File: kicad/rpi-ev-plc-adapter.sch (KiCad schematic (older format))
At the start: 51 parts, among them J1 Raspberry_RPI, J10 socket, J2 Conn_01x06, J3 header, J4 header, J5 header, J9 socket, M1 I2PLCAMN-ISE-002-T, M2 supply-5VtoPM12V_ebay-2530527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, SW1 push-button_ebay-183284526496, SW2 push-button_ebay-183284526496, SW5 dip-switch-6x2pos-smd-1.27mm

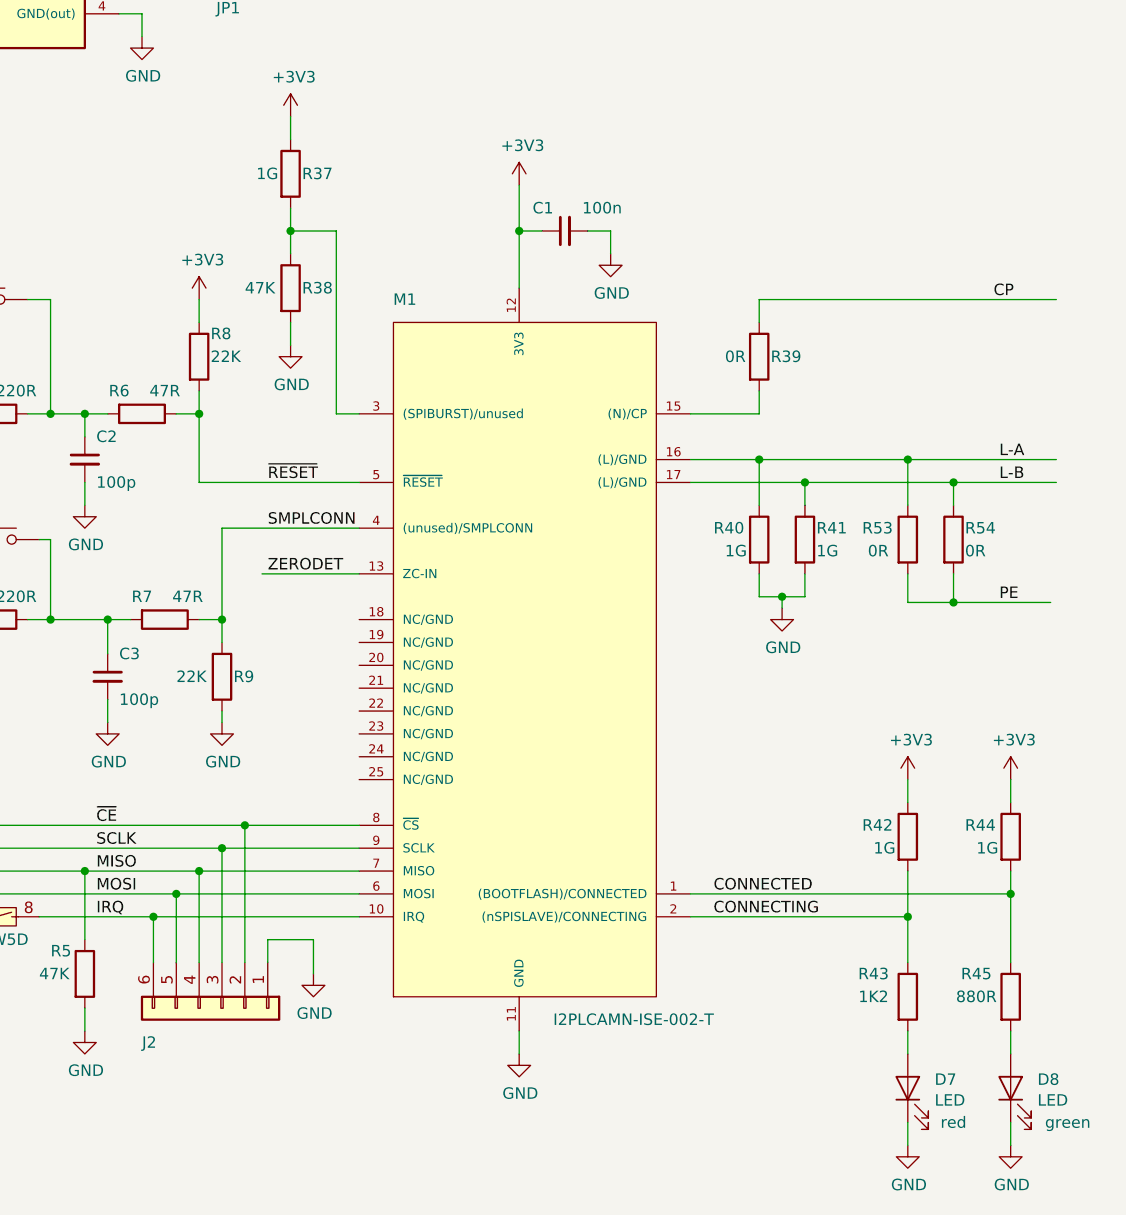
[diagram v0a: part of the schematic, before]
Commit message: pcb fix for modem with 1.27mm connector finished
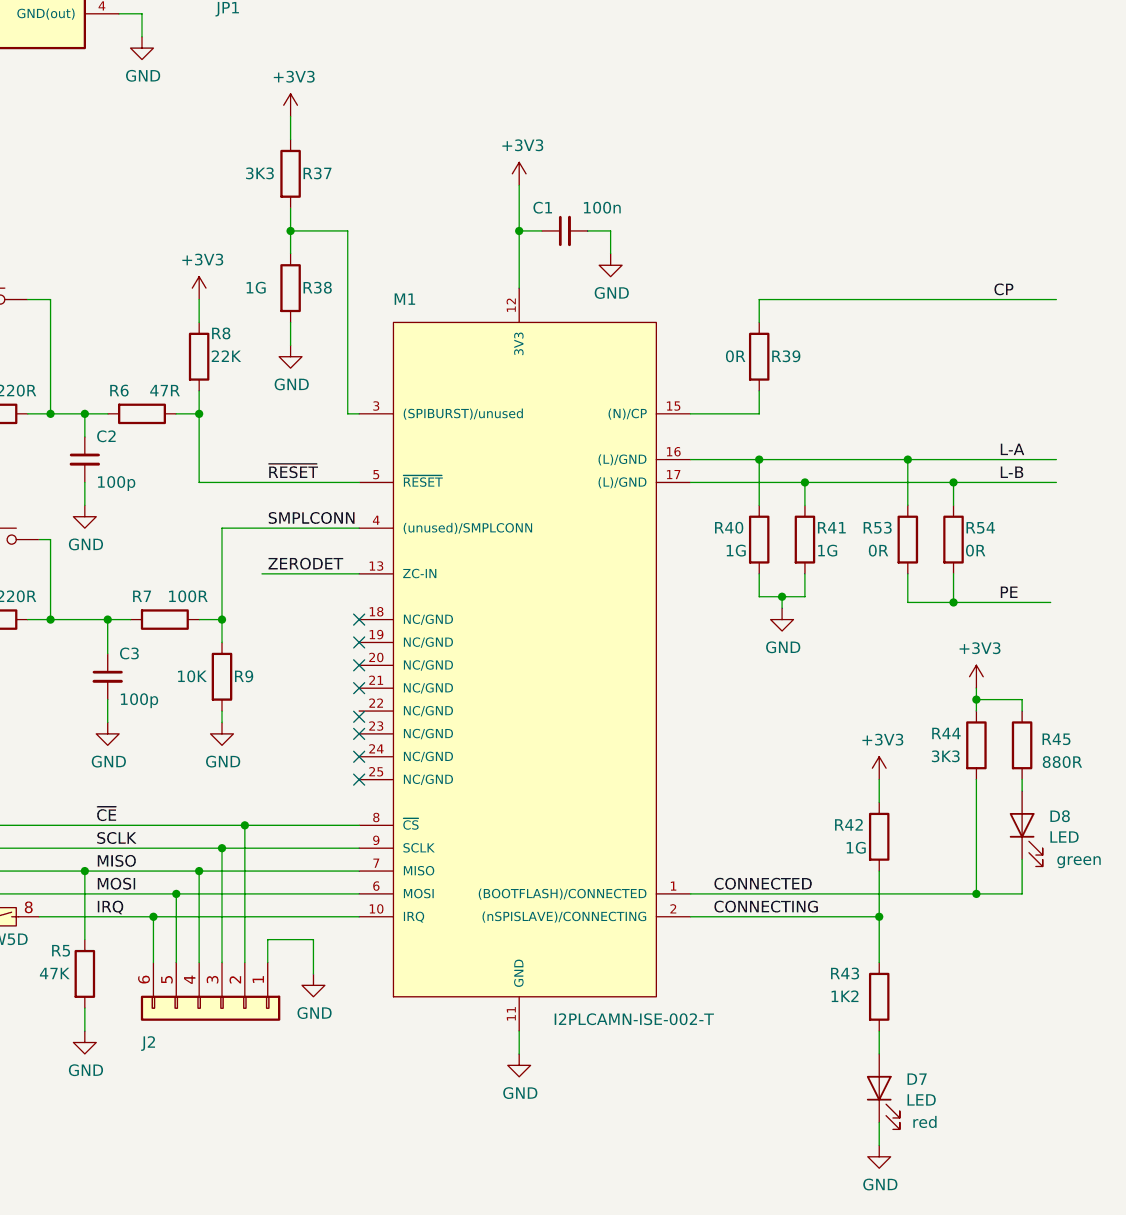
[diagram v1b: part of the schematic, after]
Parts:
- R37, R44: value 1G -> 3K3
- R38: value 47K -> 1G
- R7: value 47R -> 100R
- R9: value 22K -> 10K
- SW1, SW2: footprint Project:push-button_ebay-183284526496 -> Project:push-button-smd-4.5x4.5mm-black
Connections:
- wire segments 242 -> 245
- no-connect marks 10 -> 18
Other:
- moved on the sheet: D7, D8, R42, R43, R44, R45
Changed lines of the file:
@@
-$EndComp
-$Comp
-L project:I2PLCAMN-ISE-002-T M1
-U 1 1 5E048CF0
-P 7900 3550
-F 0 "M1" H 8100 4600 50  0000 C CNN
-F 1 "I2PLCAMN-ISE-002-T" H 9100 1450 50  0000 C CNN
-F 2 "Project:I2PLCAMN-ISE-002-T" H 8700 2250 50  0001 C CNN
-F 3 "" H 8600 2350 50  0001 C CNN
-	1    7900 3550
-	1    0    0    -1
 $EndComp
 $Comp
@@
 F 0 "SW1" H 6150 2600 50  0000 C CNN
 F 1 "push-button_ebay-183284526496" H 6250 2300 50  0001 C CNN
-F 2 "Project:push-button_ebay-183284526496" H 6250 2700 50  0001 C CNN
+F 2 "Project:push-button-smd-4.5x4.5mm-black" H 6250 2700 50  0001 C CNN
 F 3 "" H 6250 2700 50  0001 C CNN
 F 4 "black" H 6250 2400 50  0001 C CNN "color"
@@
 P 7050 3900
 F 0 "R7" V 6950 3800 50  0000 C CNN
-F 1 "47R" V 6950 4000 50  0000 C CNN
+F 1 "100R" V 6950 4000 50  0000 C CNN
 F 2 "Project:r-0805-hand-soldering" V 6980 3900 50  0001 C CNN
 F 3 "~" H 7050 3900 50  0001 C CNN
@@
 F 0 "SW2" H 6150 3650 50  0000 C CNN
 F 1 "push-button_ebay-183284526496" H 6300 3350 50  0001 C CNN
-F 2 "Project:push-button_ebay-183284526496" H 6300 3750 50  0001 C CNN
+F 2 "Project:push-button-smd-4.5x4.5mm-black" H 6300 3750 50  0001 C CNN
 F 3 "" H 6300 3750 50  0001 C CNN
 F 4 "black" H 6300 3450 50  0001 C CNN "color"
@@
 P 7300 4150
 F 0 "R9" H 7350 4150 50  0000 L CNN
-F 1 "22K" H 7100 4150 50  0000 L CNN
+F 1 "10K" H 7100 4150 50  0000 L CNN
 F 2 "Project:r-0805-hand-soldering" V 7230 4150 50  0001 C CNN
 F 3 "~" H 7300 4150 50  0001 C CNN
@@
 L Device:R R?
 U 1 1 5E2A00E2
-P 10750 5550
+P 10800 4450
 AR Path="/5E13857A/5E2A00E2" Ref="R?"  Part="1"
 AR Path="/5E2A00E2" Ref="R45"  Part="1"
-F 0 "R45" H 10600 5650 50  0000 C CNN
-F 1 "880R" H 10600 5550 50  0000 C CNN
-F 2 "Project:r-0805-hand-soldering" V 10680 5550 50  0001 C CNN
-F 3 "" H 10750 5550 50  0001 C CNN
-	1    10750 5550
+F 0 "R45" H 10950 4475 50  0000 C CNN
+F 1 "880R" H 10975 4375 50  0000 C CNN
+F 2 "Project:r-0805-hand-soldering" V 10730 4450 50  0001 C CNN
+F 3 "" H 10800 4450 50  0001 C CNN
+	1    10800 4450
 	1    0    0    -1
 $EndComp
@@
 L Device:LED D?
 U 1 1 5E2A00E9
-P 10750 5950
+P 10800 4800
 AR Path="/5E13857A/5E2A00E9" Ref="D?"  Part="1"
 AR Path="/5E2A00E9" Ref="D8"  Part="1"
-F 0 "D8" V 10788 5833 50  0000 R CNN
-F 1 "LED" V 10697 5833 50  0000 R CNN
-F 2 "LEDs:LED_0805_HandSoldering" H 10750 5950 50  0001 C CNN
-F 3 "~" H 10750 5950 50  0001 C CNN
-F 4 "green" V 10600 5700 50  0000 C CNN "color"
-	1    10750 5950
+F 0 "D8" V 10838 4683 50  0000 R CNN
+F 1 "LED" V 10747 4683 50  0000 R CNN
+F 2 "LEDs:LED_0805_HandSoldering" H 10800 4800 50  0001 C CNN
+F 3 "~" H 10800 4800 50  0001 C CNN
+F 4 "green" V 10650 4550 50  0000 C CNN "color"
+	1    10800 4800
 	0    -1   -1   0
 $EndComp
-Wire Wire Line
-	10750 5700 10750 5800
-Wire Wire Line
-	10750 5400 10750 5100
-Wire Wire Line
-	10750 5100 9350 5100
-$Comp
-L power:GND #PWR0146
-U 1 1 5E2B148A
-P 10750 6200
-F 0 "#PWR0146" H 10750 5950 50  0001 C CNN
-F 1 "GND" H 10755 6027 50  0000 C CNN
-F 2 "" H 10750 6200 50  0001 C CNN
-F 3 "" H 10750 6200 50  0001 C CNN
-	1    10750 6200
-	1    0    0    -1
-$EndComp
-Wire Wire Line
-	10750 6100 10750 6200
 $Comp
 L Device:R R?
 U 1 1 5E2C2D62
-P 10300 5550
+P 10175 5550
 AR Path="/5E13857A/5E2C2D62" Ref="R?"  Part="1"
 AR Path="/5E2C2D62" Ref="R43"  Part="1"
-F 0 "R43" H 10150 5650 50  0000 C CNN
-F 1 "1K2" H 10150 5550 50  0000 C CNN
-F 2 "Project:r-0805-hand-soldering" V 10230 5550 50  0001 C CNN
-F 3 "" H 10300 5550 50  0001 C CNN
-	1    10300 5550
+F 0 "R43" H 10025 5650 50  0000 C CNN
+F 1 "1K2" H 10025 5550 50  0000 C CNN
+F 2 "Project:r-0805-hand-soldering" V 10105 5550 50  0001 C CNN
+F 3 "" H 10175 5550 50  0001 C CNN
+	1    10175 5550
 	1    0    0    -1
 $EndComp
@@
 L Device:LED D?
 U 1 1 5E2C2D69
-P 10300 5950
+P 10175 5950
 AR Path="/5E13857A/5E2C2D69" Ref="D?"  Part="1"
 AR Path="/5E2C2D69" Ref="D7"  Part="1"
-F 0 "D7" V 10338 5833 50  0000 R CNN
-F 1 "LED" V 10247 5833 50  0000 R CNN
-F 2 "LEDs:LED_0805_HandSoldering" H 10300 5950 50  0001 C CNN
-F 3 "~" H 10300 5950 50  0001 C CNN
-F 4 "red" V 10150 5750 50  0000 C CNN "color"
-	1    10300 5950
+F 0 "D7" V 10213 5833 50  0000 R CNN
+F 1 "LED" V 10122 5833 50  0000 R CNN
+F 2 "LEDs:LED_0805_HandSoldering" H 10175 5950 50  0001 C CNN
+F 3 "~" H 10175 5950 50  0001 C CNN
+F 4 "red" V 10025 5750 50  0000 C CNN "color"
+	1    10175 5950
 	0    -1   -1   0
 $EndComp
 Wire Wire Line
-	10300 5700 10300 5800
+	10175 5700 10175 5800
 $Comp
 L power:GND #PWR0147
 U 1 1 5E2C2D71
-P 10300 6200
-F 0 "#PWR0147" H 10300 5950 50  0001 C CNN
-F 1 "GND" H 10305 6027 50  0000 C CNN
-F 2 "" H 10300 6200 50  0001 C CNN
-F 3 "" H 10300 6200 50  0001 C CNN
-	1    10300 6200
-	1    0    0    -1
-$EndComp
-Wire Wire Line
-	10300 6100 10300 6200
-Wire Wire Line
-	10300 5400 10300 5200
-Wire Wire Line
-	10300 5200 9350 5200
+P 10175 6200
+F 0 "#PWR0147" H 10175 5950 50  0001 C CNN
+F 1 "GND" H 10180 6027 50  0000 C CNN
+F 2 "" H 10175 6200 50  0001 C CNN
+F 3 "" H 10175 6200 50  0001 C CNN
+	1    10175 6200
+	1    0    0    -1
+$EndComp
+Wire Wire Line
+	10175 6100 10175 6200
 $Comp
 L Device:R R38
@@
 P 7600 2450
 F 0 "R38" H 7650 2450 50  0000 L CNN
-F 1 "47K" H 7400 2450 50  0000 L CNN
+F 1 "1G" H 7400 2450 50  0000 L CNN
 F 2 "Project:r-0805-hand-soldering" V 7530 2450 50  0001 C CNN
 F 3 "~" H 7600 2450 50  0001 C CNN
@@
 P 7600 1950
 F 0 "R37" H 7650 1950 50  0000 L CNN
-F 1 "1G" H 7450 1950 50  0000 L CNN
+F 1 "3K3" H 7400 1950 50  0000 L CNN
 F 2 "Project:r-0805-hand-soldering" V 7530 1950 50  0001 C CNN
 F 3 "~" H 7600 1950 50  0001 C CNN
@@
 	7200 3300 7900 3300
 Wire Wire Line
-	7900 3000 7800 3000
-Wire Wire Line
-	7800 3000 7800 2200
-Wire Wire Line
-	7800 2200 7600 2200
+	7900 3000 7850 3000
+Wire Wire Line
+	7850 3000 7850 2200
+Wire Wire Line
+	7850 2200 7600 2200
 Wire Wire Line
 	7600 2200 7600 2100
@@
 L Device:R R44
 U 1 1 5E32F583
-P 10750 4850
-F 0 "R44" H 10550 4900 50  0000 L CNN
-F 1 "1G" H 10600 4800 50  0000 L CNN
-F 2 "Project:r-0805-hand-soldering" V 10680 4850 50  0001 C CNN
-F 3 "~" H 10750 4850 50  0001 C CNN
-	1    10750 4850
+P 10600 4450
+F 0 "R44" H 10400 4500 50  0000 L CNN
+F 1 "3K3" H 10400 4400 50  0000 L CNN
+F 2 "Project:r-0805-hand-soldering" V 10530 4450 50  0001 C CNN
+F 3 "~" H 10600 4450 50  0001 C CNN
+	1    10600 4450
 	1    0    0    -1
 $EndComp
@@
 L Device:R R42
 U 1 1 5E32F6F3
-P 10300 4850
-F 0 "R42" H 10100 4900 50  0000 L CNN
-F 1 "1G" H 10150 4800 50  0000 L CNN
-F 2 "Project:r-0805-hand-soldering" V 10230 4850 50  0001 C CNN
-F 3 "~" H 10300 4850 50  0001 C CNN
-	1    10300 4850
+P 10175 4850
+F 0 "R42" H 9975 4900 50  0000 L CNN
+F 1 "1G" H 10025 4800 50  0000 L CNN
+F 2 "Project:r-0805-hand-soldering" V 10105 4850 50  0001 C CNN
+F 3 "~" H 10175 4850 50  0001 C CNN
+	1    10175 4850
 	1    0    0    -1
 $EndComp
@@
 L power:+3V3 #PWR0150
 U 1 1 5E32F818
-P 10750 4600
-F 0 "#PWR0150" H 10750 4450 50  0001 C CNN
-F 1 "+3V3" H 10765 4773 50  0000 C CNN
-F 2 "" H 10750 4600 50  0001 C CNN
-F 3 "" H 10750 4600 50  0001 C CNN
-	1    10750 4600
+P 10600 4200
+F 0 "#PWR0150" H 10600 4050 50  0001 C CNN
+F 1 "+3V3" H 10615 4373 50  0000 C CNN
+F 2 "" H 10600 4200 50  0001 C CNN
+F 3 "" H 10600 4200 50  0001 C CNN
+	1    10600 4200
 	1    0    0    -1
 $EndComp
@@
 L power:+3V3 #PWR0151
 U 1 1 5E32F8DC
-P 10300 4600
-F 0 "#PWR0151" H 10300 4450 50  0001 C CNN
-F 1 "+3V3" H 10315 4773 50  0000 C CNN
-F 2 "" H 10300 4600 50  0001 C CNN
-F 3 "" H 10300 4600 50  0001 C CNN
-	1    10300 4600
-	1    0    0    -1
-$EndComp
-Wire Wire Line
-	10300 4700 10300 4600
-Wire Wire Line
-	10750 4700 10750 4600
-Wire Wire Line
-	10300 5200 10300 5000
-Connection ~ 10300 5200
-Wire Wire Line
-	10750 5100 10750 5000
-Connection ~ 10750 5100
+P 10175 4600
+F 0 "#PWR0151" H 10175 4450 50  0001 C CNN
+F 1 "+3V3" H 10190 4773 50  0000 C CNN
+F 2 "" H 10175 4600 50  0001 C CNN
+F 3 "" H 10175 4600 50  0001 C CNN
+	1    10175 4600
+	1    0    0    -1
+$EndComp
+Wire Wire Line
+	10175 4700 10175 4600
+Wire Wire Line
+	10600 4300 10600 4250
 Text Label 9450 5100 0    50   ~ 0
 CONNECTED
@@
 Wire Wire Line
 	7900 1150 8900 1150
+$Comp
+L project:I2PLCAMN-ISE-002-T M1
+U 1 1 5E048CF0
+P 7900 3550
+F 0 "M1" H 8100 4600 50  0000 C CNN
+F 1 "I2PLCAMN-ISE-002-T" H 9100 1450 50  0000 C CNN
+F 2 "Project:I2PLCAMN-ISE-002-T" H 8700 2250 50  0001 C CNN
+F 3 "" H 8600 2350 50  0001 C CNN
+	1    7900 3550
+	1    0    0    -1
+$EndComp
+Wire Wire Line
+	10600 4250 10800 4250
+Wire Wire Line
+	10800 4250 10800 4300
+Connection ~ 10600 4250
+Wire Wire Line
+	10600 4250 10600 4200
+Wire Wire Line
+	10800 4650 10800 4600
+Wire Wire Line
+	10800 5100 10800 4950
+Wire Wire Line
+	10600 4600 10600 5100
+Wire Wire Line
+	10600 5100 10800 5100
+Wire Wire Line
+	10175 5000 10175 5200
+Wire Wire Line
+	9350 5100 10600 5100
+Connection ~ 10600 5100
+Wire Wire Line
+	9350 5200 10175 5200
+Connection ~ 10175 5200
+Wire Wire Line
+	10175 5200 10175 5400
+NoConn ~ 7900 3900
+NoConn ~ 7900 4000
+NoConn ~ 7900 4100
+NoConn ~ 7900 4200
+NoConn ~ 7900 4325
+NoConn ~ 7900 4400
+NoConn ~ 7900 4500
+NoConn ~ 7900 4600
 $EndSCHEMATC

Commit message: schematic/pcb V1.0 finished
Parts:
- removed R49, R50: 220R, Project:r-0805-hand-soldering, symbol Device:R
- removed SW5: dip-switch-6x2pos-smd-1.27mm, Project:dip-switch-6x2pos-smd-1.27mm, symbol project:dip-switch-6x2pos-smd-1.27mm
- added SW5: dip-switch-4x2pos-smd-1.27mm, Project:dip-switch-4x2pos-smd-1.27mm, symbol project:dip-switch-4x2pos-smd-1.27mm
- R1, R2, R3, R36, R37, R38, R39, R4, R40, R41, R42, R43, R44, R45, R46, R47, R5, R51, R52, R53, R54, R6, R7, R8, R9: footprint Project:r-0805-hand-soldering -> Project:r-1206-hand-soldering
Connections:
- net labels added: PI-IRQ, PI-PWM, RECONN, SPIBURST, ~PLC-RES
- wire segments 245 -> 253
- no-connect marks 18 -> 12
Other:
- moved on the sheet: C2, R3, R4, R6, R8

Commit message: Checks/Fixxes done, V1.0 ready for tape out
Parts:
- added J7, J8: header, Project:idc-header-1x02-p2.54mm-vertical, symbol Connector_Generic:Conn_01x02
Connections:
- wire segments 253 -> 262
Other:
- moved on the sheet: D12, R51
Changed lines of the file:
@@
 encoding utf-8
 Sheet 1 2
-Title ""
-Date ""
-Rev ""
-Comp ""
-Comment1 ""
+Title "RPI-EV-PLC Adapter"
+Date "2020-02-14"
+Rev "V1.0"
+Comp "(C) Manfred Steiner"
+Comment1 "https://github.com/greenenergyprojects/rpi-ev-plc-adapter"
 Comment2 ""
 Comment3 ""
@@
 L power:+5V #PWR0104
 U 1 1 5E04B2E6
-P 5750 950
-F 0 "#PWR0104" H 5750 800 50  0001 C CNN
-F 1 "+5V" H 5765 1123 50  0000 C CNN
-F 2 "" H 5750 950 50  0001 C CNN
-F 3 "" H 5750 950 50  0001 C CNN
-	1    5750 950
+P 5750 700
+F 0 "#PWR0104" H 5750 550 50  0001 C CNN
+F 1 "+5V" H 5765 873 50  0000 C CNN
+F 2 "" H 5750 700 50  0001 C CNN
+F 3 "" H 5750 700 50  0001 C CNN
+	1    5750 700
 	1    0    0    -1
 $EndComp
@@
 	5850 1050 5750 1050
 Wire Wire Line
-	5750 1050 5750 950
+	5750 1050 5750 750
 $Comp
 L power:GND #PWR0106
@@
 L power:+5V #PWR0109
 U 1 1 5E04B9EF
-P 4900 1750
-F 0 "#PWR0109" H 4900 1600 50  0001 C CNN
-F 1 "+5V" H 4915 1923 50  0000 C CNN
-F 2 "" H 4900 1750 50  0001 C CNN
-F 3 "" H 4900 1750 50  0001 C CNN
-	1    4900 1750
+P 4900 1825
+F 0 "#PWR0109" H 4900 1675 50  0001 C CNN
+F 1 "+5V" H 4915 1998 50  0000 C CNN
+F 2 "" H 4900 1825 50  0001 C CNN
+F 3 "" H 4900 1825 50  0001 C CNN
+	1    4900 1825
 	1    0    0    -1
 $EndComp
@@
 	4950 1900 4950 2000
 Wire Wire Line
-	4900 1900 4900 1750
+	4900 1900 4900 1825
 Connection ~ 4900 1900
 Wire Wire Line
@@
 L power:GND #PWR0160
 U 1 1 5E7AE876
-P 5150 1350
-F 0 "#PWR0160" H 5150 1100 50  0001 C CNN
-F 1 "GND" H 5155 1177 50  0000 C CNN
-F 2 "" H 5150 1350 50  0001 C CNN
-F 3 "" H 5150 1350 50  0001 C CNN
-	1    5150 1350
-	1    0    0    -1
-$EndComp
-Wire Wire Line
-	5150 1300 5150 1350
+P 3850 1350
+F 0 "#PWR0160" H 3850 1100 50  0001 C CNN
+F 1 "GND" H 3855 1177 50  0000 C CNN
+F 2 "" H 3850 1350 50  0001 C CNN
+F 3 "" H 3850 1350 50  0001 C CNN
+	1    3850 1350
+	1    0    0    -1
+$EndComp
+Wire Wire Line
+	3850 1300 3850 1350
 $Comp
 L Device:LED D?
 U 1 1 5E7AE86E
-P 5150 1150
+P 3850 1150
 AR Path="/5E13857A/5E7AE86E" Ref="D?"  Part="1"
 AR Path="/5E7AE86E" Ref="D12"  Part="1"
-F 0 "D12" V 5188 1033 50  0000 R CNN
-F 1 "LED" V 5097 1033 50  0000 R CNN
-F 2 "LEDs:LED_0805_HandSoldering" H 5150 1150 50  0001 C CNN
-F 3 "~" H 5150 1150 50  0001 C CNN
-F 4 "green" V 5000 950 50  0000 C CNN "color"
-	1    5150 1150
+F 0 "D12" V 3888 1033 50  0000 R CNN
+F 1 "LED" V 3797 1033 50  0000 R CNN
+F 2 "LEDs:LED_0805_HandSoldering" H 3850 1150 50  0001 C CNN
+F 3 "~" H 3850 1150 50  0001 C CNN
+F 4 "green" V 3700 950 50  0000 C CNN "color"
+	1    3850 1150
 	0    -1   -1   0
 $EndComp
@@
 L Device:R R51
 U 1 1 5E7CD3EB
-P 4800 950
-F 0 "R51" V 4700 850 50  0000 C CNN
-F 1 "880R" V 4700 1050 50  0000 C CNN
-F 2 "Project:r-1206-hand-soldering" V 4730 950 50  0001 C CNN
-F 3 "~" H 4800 950 50  0001 C CNN
-	1    4800 950
-	0    1    1    0
-$EndComp
-Wire Wire Line
-	4400 950  4650 950
-Wire Wire Line
-	4950 950  5150 950
+P 4150 950
+F 0 "R51" V 4050 1050 50  0000 C CNN
+F 1 "880R" V 4050 850 50  0000 C CNN
+F 2 "Project:r-1206-hand-soldering" V 4080 950 50  0001 C CNN
+F 3 "~" H 4150 950 50  0001 C CNN
+	1    4150 950
+	0    -1   1    0
+$EndComp
 Wire Wire Line
 	4400 950  4400 850
 Wire Wire Line
-	5150 1000 5150 950
+	3850 1000 3850 950
 Wire Wire Line
 	5600 5000 6700 5000
@@
 M-12V
 Wire Wire Line
-	4400 950  4400 1900
+	4400 950  4400 1100
 Wire Wire Line
 	1900 3000 1700 3000
@@
 	7725 4600 7725 4500
 Connection ~ 7725 4500
+$Comp
+L Connector_Generic:Conn_01x02 J7
+U 1 1 5E481FEB
+P 5200 850
+F 0 "J7" H 5225 650 50  0000 C CNN
+F 1 "header" H 5225 950 50  0000 C CNN
+F 2 "Project:idc-header-1x02-p2.54mm-vertical" H 5200 850 50  0001 C CNN
+F 3 "~" H 5200 850 50  0001 C CNN
+	1    5200 850
+	-1   0    0    1
+$EndComp
+Wire Wire Line
+	4000 950  3850 950
+Wire Wire Line
+	4400 950  4300 950
+Wire Wire Line
+	5750 750  5400 750
+Connection ~ 5750 750
+Wire Wire Line
+	5750 750  5750 700
+Wire Wire Line
+	5400 850  5500 850
+Wire Wire Line
+	5500 850  5500 1250
+Wire Wire Line
+	5500 1250 5750 1250
+Connection ~ 5750 1250
+$Comp
+L Connector_Generic:Conn_01x02 J8
+U 1 1 5E55E445
+P 4800 1200
+F 0 "J8" H 4825 1000 50  0000 C CNN
+F 1 "header" H 4825 1300 50  0000 C CNN
+F 2 "Project:idc-header-1x02-p2.54mm-vertical" H 4800 1200 50  0001 C CNN
+F 3 "~" H 4800 1200 50  0001 C CNN
+	1    4800 1200
+	1    0    0    1
+$EndComp
+Wire Wire Line
+	4600 1100 4400 1100
+Connection ~ 4400 1100
+Wire Wire Line
+	4400 1100 4400 1900
+$Comp
+L power:GND #PWR0145
+U 1 1 5E581ACC
+P 4550 1300
+F 0 "#PWR0145" H 4550 1050 50  0001 C CNN
+F 1 "GND" H 4555 1127 50  0000 C CNN
+F 2 "" H 4550 1300 50  0001 C CNN
+F 3 "" H 4550 1300 50  0001 C CNN
+	1    4550 1300
+	1    0    0    -1
+$EndComp
+Wire Wire Line
+	4550 1300 4550 1200
+Wire Wire Line
+	4550 1200 4600 1200
 $EndSCHEMATC
